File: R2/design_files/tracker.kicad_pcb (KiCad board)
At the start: 4 copper layers, 49.4 x 53.4 mm, 95 parts, among them J1 Conn_01x01, J2 Conn_01x01, J3 Conn_01x05, J4 Conn_Coaxial, J5 SIM_Card, J6 Conn_01x02, M1 BG96, Q1 DMP2008UFG, U1 STM32U545CEUx, U10 PUMH10,115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

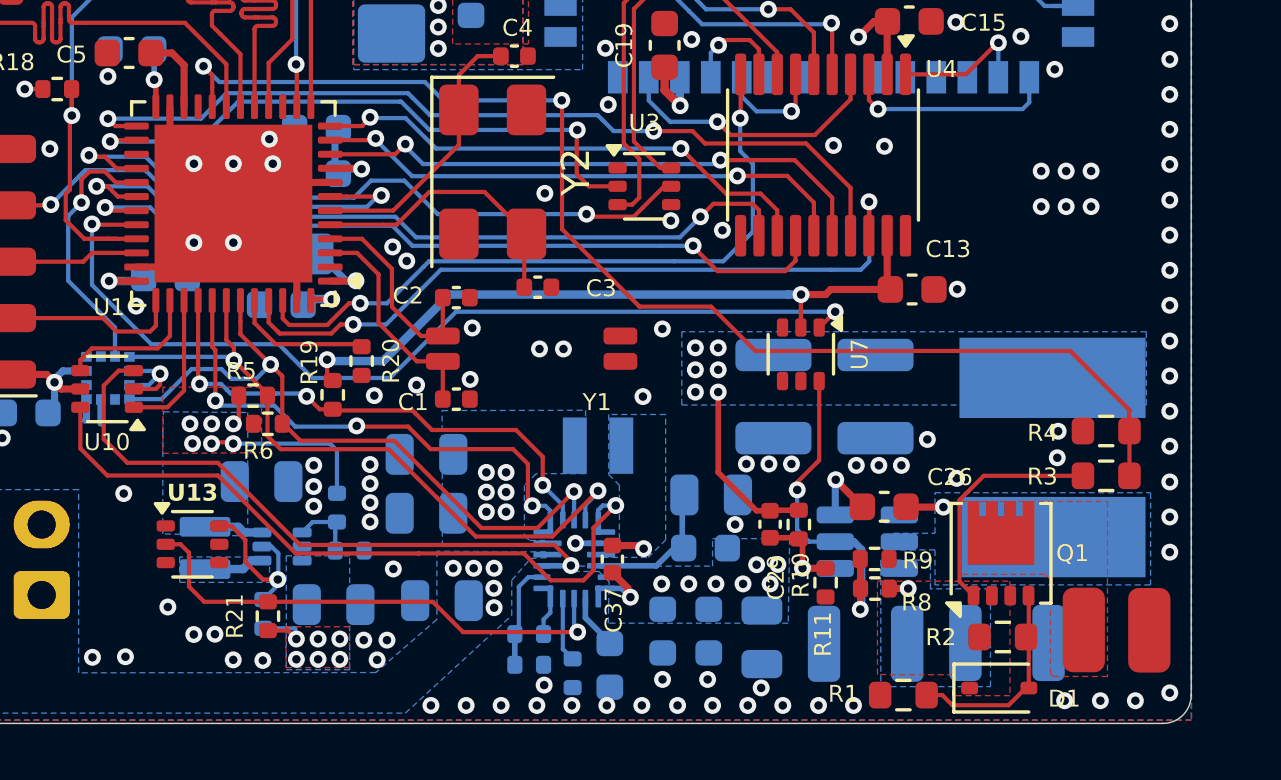
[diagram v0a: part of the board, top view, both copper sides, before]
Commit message: Added test points
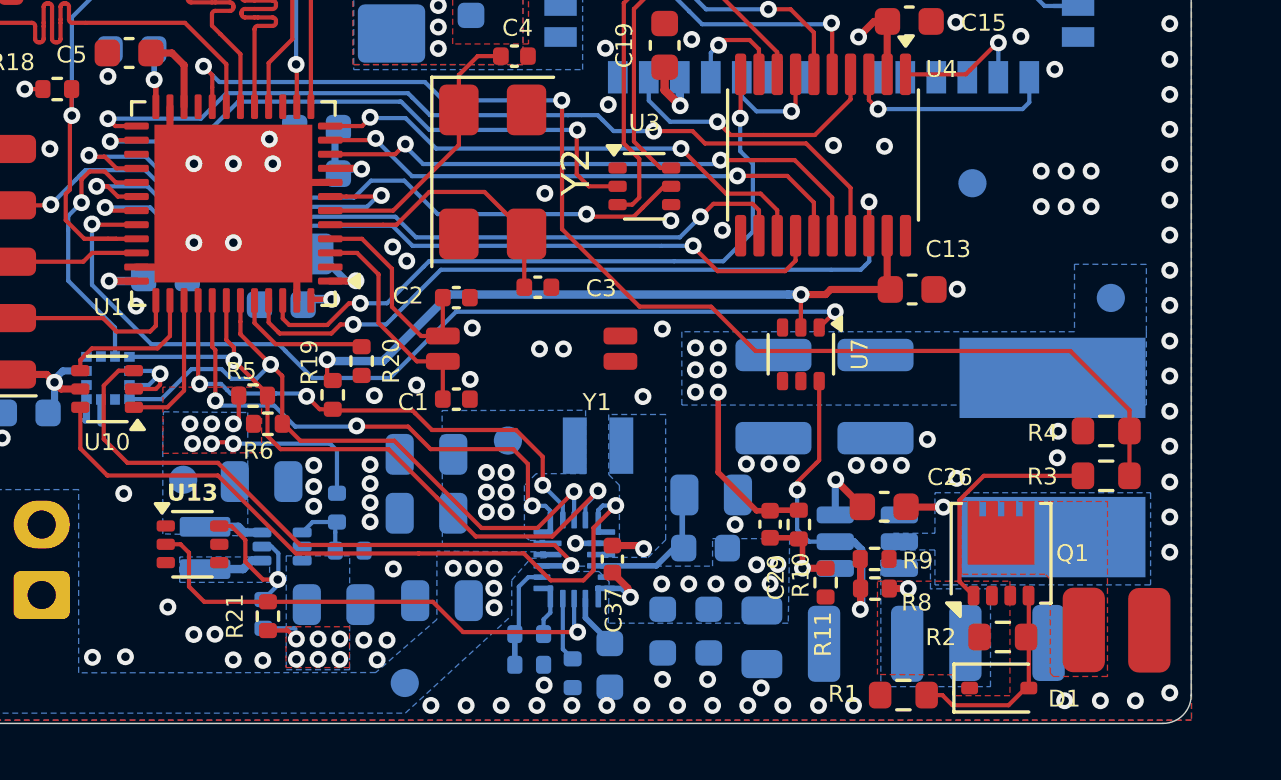
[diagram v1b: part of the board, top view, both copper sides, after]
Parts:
- added TP1: TestPoint, TestPoint:TestPoint_Pad_D1.0mm, B.Cu at (147.7, 86.5)
- added TP2: TestPoint, TestPoint:TestPoint_Pad_D1.0mm, B.Cu at (144.1, 95.1)
- added TP3: TestPoint, TestPoint:TestPoint_Pad_D1.0mm, B.Cu at (164.2, 77.4)
- added TP4: TestPoint, TestPoint:TestPoint_Pad_D1.0mm, B.Cu at (136.2, 87.9)
- added TP5: TestPoint, TestPoint:TestPoint_Pad_D1.0mm, B.Cu at (169.1, 81.5)
- U11: value ~ -> BQ25622E
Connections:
- net +2V8 renamed +1V8
- U13 pad 1: unconnected-(U13-Pad1) -> GND
- U4 pad 20: /gsm/GSM_STATUS -> unconnected-(U4-B1-Pad20)
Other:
- board text added: "+3V3"
- board text added: "+5V"
- board text added: "+VBAT"
- board text added: "+VSYS"
- board text added: "GND"
